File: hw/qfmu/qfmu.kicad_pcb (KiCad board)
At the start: 2 copper layers, 1 part, among them U1 EFM32GG11B120F2048GQ64

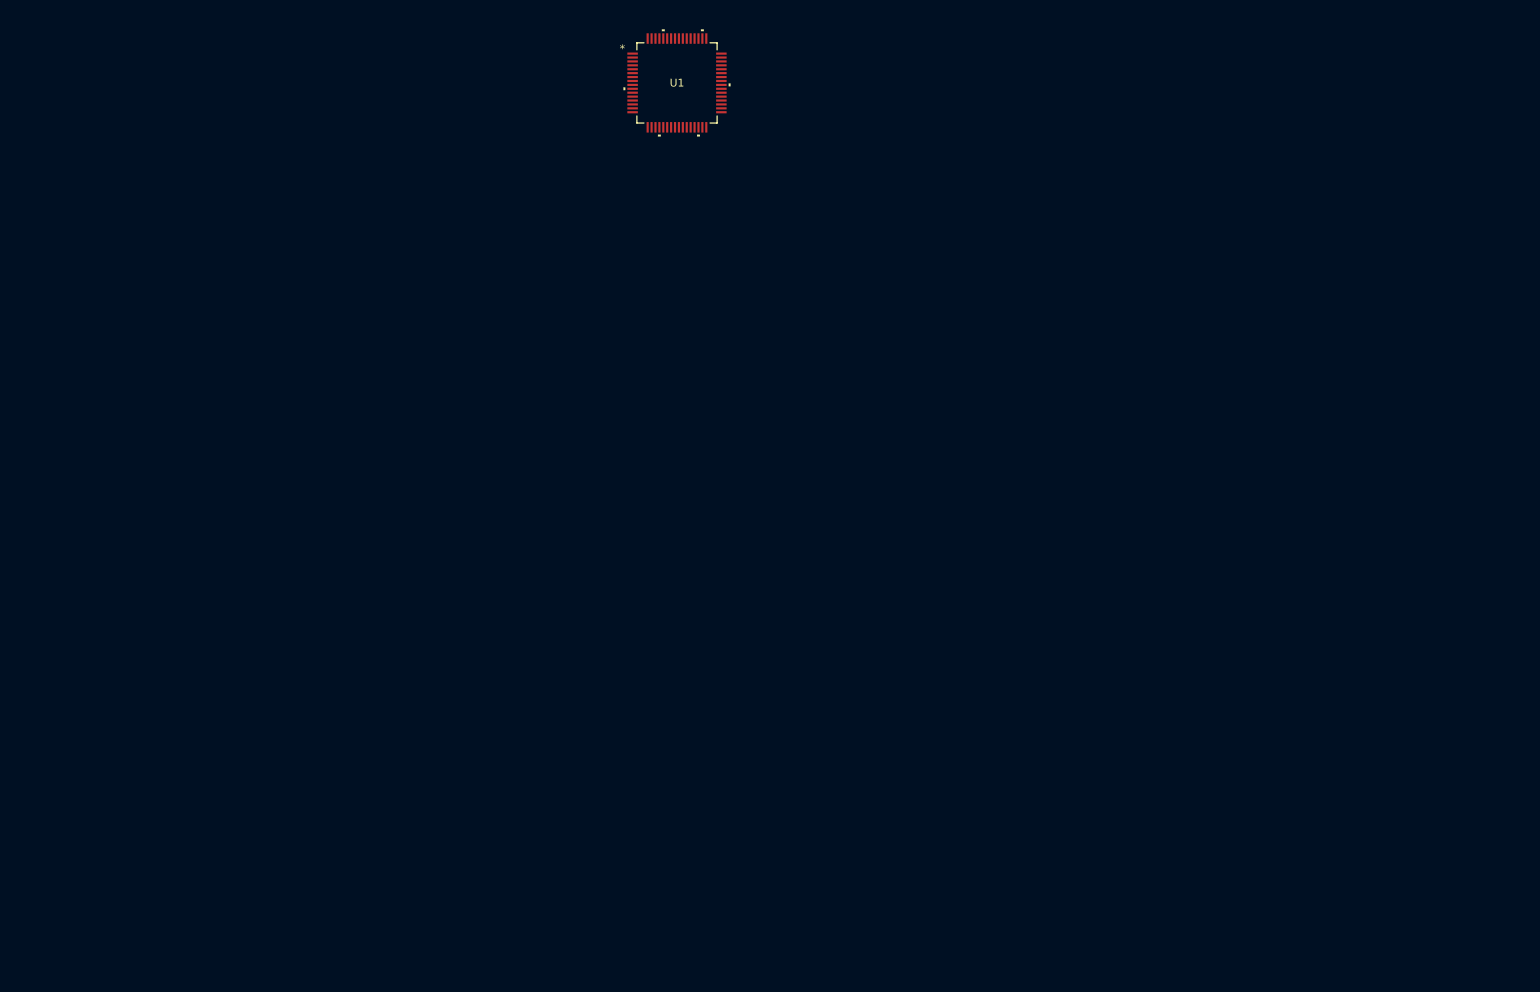
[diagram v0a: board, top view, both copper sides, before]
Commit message: feat: add new BLDC controler and RF section
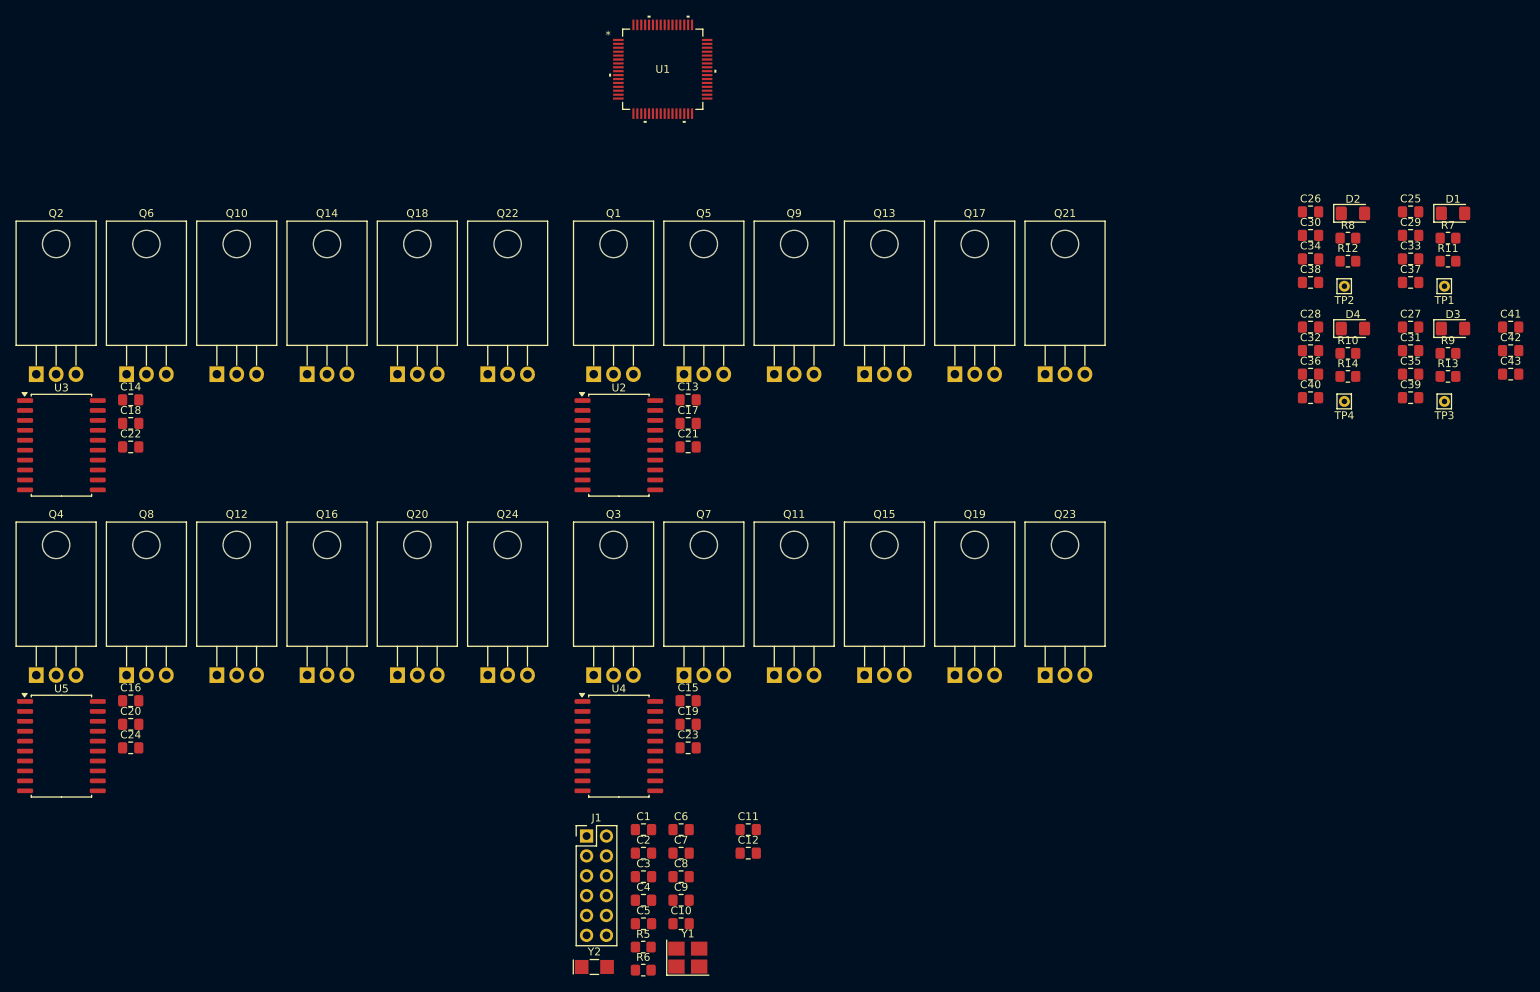
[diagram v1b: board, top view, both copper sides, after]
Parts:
- added C1: 1u, Capacitor_SMD:C_0805_2012Metric_Pad1.18x1.45mm_HandSolder, F.Cu at (132.5, 159.8)
- added C10: 1u, Capacitor_SMD:C_0805_2012Metric_Pad1.18x1.45mm_HandSolder, F.Cu at (137.3, 171.8)
- added C11: 0.1u, Capacitor_SMD:C_0805_2012Metric_Pad1.18x1.45mm_HandSolder, F.Cu at (145.9, 159.8)
- added C12: 0.1u, Capacitor_SMD:C_0805_2012Metric_Pad1.18x1.45mm_HandSolder, F.Cu at (145.9, 162.8)
- added C13: 1u, Capacitor_SMD:C_0805_2012Metric_Pad1.18x1.45mm_HandSolder, F.Cu at (138.2, 104.8)
- added C14: 1u, Capacitor_SMD:C_0805_2012Metric_Pad1.18x1.45mm_HandSolder, F.Cu at (67.0, 104.8)
- added C15: 1u, Capacitor_SMD:C_0805_2012Metric_Pad1.18x1.45mm_HandSolder, F.Cu at (138.2, 143.3)
- added C16: 1u, Capacitor_SMD:C_0805_2012Metric_Pad1.18x1.45mm_HandSolder, F.Cu at (67.0, 143.3)
- added C17: 1u, Capacitor_SMD:C_0805_2012Metric_Pad1.18x1.45mm_HandSolder, F.Cu at (138.2, 107.8)
- added C18: 1u, Capacitor_SMD:C_0805_2012Metric_Pad1.18x1.45mm_HandSolder, F.Cu at (67.0, 107.8)
- added C19: 1u, Capacitor_SMD:C_0805_2012Metric_Pad1.18x1.45mm_HandSolder, F.Cu at (138.2, 146.3)
- added C2: 0.1u, Capacitor_SMD:C_0805_2012Metric_Pad1.18x1.45mm_HandSolder, F.Cu at (132.5, 162.8)
- added C20: 1u, Capacitor_SMD:C_0805_2012Metric_Pad1.18x1.45mm_HandSolder, F.Cu at (67.0, 146.3)
- added C21: 10n, Capacitor_SMD:C_0805_2012Metric_Pad1.18x1.45mm_HandSolder, F.Cu at (138.2, 110.8)
- added C22: 10n, Capacitor_SMD:C_0805_2012Metric_Pad1.18x1.45mm_HandSolder, F.Cu at (67.0, 110.8)
- added C23: 10n, Capacitor_SMD:C_0805_2012Metric_Pad1.18x1.45mm_HandSolder, F.Cu at (138.2, 149.3)
- added C24: 10n, Capacitor_SMD:C_0805_2012Metric_Pad1.18x1.45mm_HandSolder, F.Cu at (67.0, 149.3)
- added C25: 2.2n, Capacitor_SMD:C_0805_2012Metric_Pad1.18x1.45mm_HandSolder, F.Cu at (230.7, 80.7)
- added C26: 2.2n, Capacitor_SMD:C_0805_2012Metric_Pad1.18x1.45mm_HandSolder, F.Cu at (217.9, 80.7)
- added C27: 2.2n, Capacitor_SMD:C_0805_2012Metric_Pad1.18x1.45mm_HandSolder, F.Cu at (230.7, 95.5)
- added C28: 2.2n, Capacitor_SMD:C_0805_2012Metric_Pad1.18x1.45mm_HandSolder, F.Cu at (217.9, 95.5)
- added C29: 4.7n, Capacitor_SMD:C_0805_2012Metric_Pad1.18x1.45mm_HandSolder, F.Cu at (230.7, 83.8)
- added C3: 10u, Capacitor_SMD:C_0805_2012Metric_Pad1.18x1.45mm_HandSolder, F.Cu at (132.5, 165.8)
- added C30: 4.7n, Capacitor_SMD:C_0805_2012Metric_Pad1.18x1.45mm_HandSolder, F.Cu at (217.9, 83.8)
- added C31: 4.7n, Capacitor_SMD:C_0805_2012Metric_Pad1.18x1.45mm_HandSolder, F.Cu at (230.7, 98.5)
- added C32: 4.7n, Capacitor_SMD:C_0805_2012Metric_Pad1.18x1.45mm_HandSolder, F.Cu at (217.9, 98.5)
- added C33: 4.7n, Capacitor_SMD:C_0805_2012Metric_Pad1.18x1.45mm_HandSolder, F.Cu at (230.7, 86.8)
- added C34: 4.7n, Capacitor_SMD:C_0805_2012Metric_Pad1.18x1.45mm_HandSolder, F.Cu at (217.9, 86.8)
- added C35: 4.7n, Capacitor_SMD:C_0805_2012Metric_Pad1.18x1.45mm_HandSolder, F.Cu at (230.7, 101.5)
- added C36: 4.7n, Capacitor_SMD:C_0805_2012Metric_Pad1.18x1.45mm_HandSolder, F.Cu at (217.9, 101.5)
- added C37: 4.7n, Capacitor_SMD:C_0805_2012Metric_Pad1.18x1.45mm_HandSolder, F.Cu at (230.7, 89.8)
- added C38: 4.7n, Capacitor_SMD:C_0805_2012Metric_Pad1.18x1.45mm_HandSolder, F.Cu at (217.9, 89.8)
- added C39: 4.7n, Capacitor_SMD:C_0805_2012Metric_Pad1.18x1.45mm_HandSolder, F.Cu at (230.7, 104.5)
- added C4: 10n, Capacitor_SMD:C_0805_2012Metric_Pad1.18x1.45mm_HandSolder, F.Cu at (132.5, 168.8)
- added C40: 4.7n, Capacitor_SMD:C_0805_2012Metric_Pad1.18x1.45mm_HandSolder, F.Cu at (217.9, 104.5)
- added C41: 0.1u, Capacitor_SMD:C_0805_2012Metric_Pad1.18x1.45mm_HandSolder, F.Cu at (243.5, 95.5)
- added C42: 0.1u, Capacitor_SMD:C_0805_2012Metric_Pad1.18x1.45mm_HandSolder, F.Cu at (243.5, 98.5)
- added C43: 1u, Capacitor_SMD:C_0805_2012Metric_Pad1.18x1.45mm_HandSolder, F.Cu at (243.5, 101.5)
- added C5: 10u, Capacitor_SMD:C_0805_2012Metric_Pad1.18x1.45mm_HandSolder, F.Cu at (132.5, 171.8)
- added C6: 10n, Capacitor_SMD:C_0805_2012Metric_Pad1.18x1.45mm_HandSolder, F.Cu at (137.3, 159.8)
- added C7: 0.1u, Capacitor_SMD:C_0805_2012Metric_Pad1.18x1.45mm_HandSolder, F.Cu at (137.3, 162.8)
- added C8: 1u, Capacitor_SMD:C_0805_2012Metric_Pad1.18x1.45mm_HandSolder, F.Cu at (137.3, 165.8)
- added C9: 0.1u, Capacitor_SMD:C_0805_2012Metric_Pad1.18x1.45mm_HandSolder, F.Cu at (137.3, 168.8)
- added D1: LED, LED_SMD:LED_1206_3216Metric_Pad1.42x1.75mm_HandSolder, F.Cu at (236.1, 80.9)
- added D2: LED, LED_SMD:LED_1206_3216Metric_Pad1.42x1.75mm_HandSolder, F.Cu at (223.3, 80.9)
- added D3: LED, LED_SMD:LED_1206_3216Metric_Pad1.42x1.75mm_HandSolder, F.Cu at (236.1, 95.7)
- added D4: LED, LED_SMD:LED_1206_3216Metric_Pad1.42x1.75mm_HandSolder, F.Cu at (223.3, 95.7)
- added J1: Conn_02x06_Counter_Clockwise, Connector_PinHeader_2.54mm:PinHeader_2x06_P2.54mm_Vertical, F.Cu at (125.3, 160.6)
- added Q1: IRF540N, Package_TO_SOT_THT:TO-220-3_Horizontal_TabDown, F.Cu at (126.2, 101.5)
- added Q10: IRF540N, Package_TO_SOT_THT:TO-220-3_Horizontal_TabDown, F.Cu at (78.0, 101.5)
- added Q11: IRF540N, Package_TO_SOT_THT:TO-220-3_Horizontal_TabDown, F.Cu at (149.3, 140.0)
- added Q12: IRF540N, Package_TO_SOT_THT:TO-220-3_Horizontal_TabDown, F.Cu at (78.0, 140.0)
- added Q13: IRF540N, Package_TO_SOT_THT:TO-220-3_Horizontal_TabDown, F.Cu at (160.8, 101.5)
- added Q14: IRF540N, Package_TO_SOT_THT:TO-220-3_Horizontal_TabDown, F.Cu at (89.5, 101.5)
- added Q15: IRF540N, Package_TO_SOT_THT:TO-220-3_Horizontal_TabDown, F.Cu at (160.8, 140.0)
- added Q16: IRF540N, Package_TO_SOT_THT:TO-220-3_Horizontal_TabDown, F.Cu at (89.5, 140.0)
- added Q17: IRF540N, Package_TO_SOT_THT:TO-220-3_Horizontal_TabDown, F.Cu at (172.4, 101.5)
- added Q18: IRF540N, Package_TO_SOT_THT:TO-220-3_Horizontal_TabDown, F.Cu at (101.1, 101.5)
- added Q19: IRF540N, Package_TO_SOT_THT:TO-220-3_Horizontal_TabDown, F.Cu at (172.4, 140.0)
- added Q2: IRF540N, Package_TO_SOT_THT:TO-220-3_Horizontal_TabDown, F.Cu at (54.9, 101.5)
- added Q20: IRF540N, Package_TO_SOT_THT:TO-220-3_Horizontal_TabDown, F.Cu at (101.1, 140.0)
- added Q21: IRF540N, Package_TO_SOT_THT:TO-220-3_Horizontal_TabDown, F.Cu at (183.9, 101.5)
- added Q22: IRF540N, Package_TO_SOT_THT:TO-220-3_Horizontal_TabDown, F.Cu at (112.6, 101.5)
- added Q23: IRF540N, Package_TO_SOT_THT:TO-220-3_Horizontal_TabDown, F.Cu at (183.9, 140.0)
- added Q24: IRF540N, Package_TO_SOT_THT:TO-220-3_Horizontal_TabDown, F.Cu at (112.6, 140.0)
- added Q3: IRF540N, Package_TO_SOT_THT:TO-220-3_Horizontal_TabDown, F.Cu at (126.2, 140.0)
- added Q4: IRF540N, Package_TO_SOT_THT:TO-220-3_Horizontal_TabDown, F.Cu at (54.9, 140.0)
- added Q5: IRF540N, Package_TO_SOT_THT:TO-220-3_Horizontal_TabDown, F.Cu at (137.7, 101.5)
- added Q6: IRF540N, Package_TO_SOT_THT:TO-220-3_Horizontal_TabDown, F.Cu at (66.4, 101.5)
- added Q7: IRF540N, Package_TO_SOT_THT:TO-220-3_Horizontal_TabDown, F.Cu at (137.7, 140.0)
- added Q8: IRF540N, Package_TO_SOT_THT:TO-220-3_Horizontal_TabDown, F.Cu at (66.4, 140.0)
- added Q9: IRF540N, Package_TO_SOT_THT:TO-220-3_Horizontal_TabDown, F.Cu at (149.3, 101.5)
- added R10: 4.7k, Resistor_SMD:R_0805_2012Metric_Pad1.20x1.40mm_HandSolder, F.Cu at (222.6, 98.8)
- added R11: 4.7k, Resistor_SMD:R_0805_2012Metric_Pad1.20x1.40mm_HandSolder, F.Cu at (235.4, 87.0)
- added R12: 4.7k, Resistor_SMD:R_0805_2012Metric_Pad1.20x1.40mm_HandSolder, F.Cu at (222.6, 87.0)
- added R13: 4.7k, Resistor_SMD:R_0805_2012Metric_Pad1.20x1.40mm_HandSolder, F.Cu at (235.4, 101.8)
- added R14: 4.7k, Resistor_SMD:R_0805_2012Metric_Pad1.20x1.40mm_HandSolder, F.Cu at (222.6, 101.8)
- added R5: 4.7k, Resistor_SMD:R_0805_2012Metric_Pad1.20x1.40mm_HandSolder, F.Cu at (132.5, 174.8)
- added R6: 4.7k, Resistor_SMD:R_0805_2012Metric_Pad1.20x1.40mm_HandSolder, F.Cu at (132.5, 177.7)
- added R7: 4.7k, Resistor_SMD:R_0805_2012Metric_Pad1.20x1.40mm_HandSolder, F.Cu at (235.4, 84.1)
- added R8: 4.7k, Resistor_SMD:R_0805_2012Metric_Pad1.20x1.40mm_HandSolder, F.Cu at (222.6, 84.1)
- added R9: 4.7k, Resistor_SMD:R_0805_2012Metric_Pad1.20x1.40mm_HandSolder, F.Cu at (235.4, 98.8)
- added TP1: TestPoint, Connector_Pin:Pin_D0.7mm_L6.5mm_W1.8mm_FlatFork, F.Cu at (235.0, 90.2)
- added TP2: TestPoint, Connector_Pin:Pin_D0.7mm_L6.5mm_W1.8mm_FlatFork, F.Cu at (222.2, 90.2)
- added TP3: TestPoint, Connector_Pin:Pin_D0.7mm_L6.5mm_W1.8mm_FlatFork, F.Cu at (235.0, 105.0)
- added TP4: TestPoint, Connector_Pin:Pin_D0.7mm_L6.5mm_W1.8mm_FlatFork, F.Cu at (222.2, 105.0)
- added U2: FAN7888, Package_SO:SOIC-20W_7.5x12.8mm_P1.27mm, F.Cu at (129.4, 110.6)
- added U3: FAN7888, Package_SO:SOIC-20W_7.5x12.8mm_P1.27mm, F.Cu at (58.1, 110.6)
- added U4: FAN7888, Package_SO:SOIC-20W_7.5x12.8mm_P1.27mm, F.Cu at (129.4, 149.1)
- added U5: FAN7888, Package_SO:SOIC-20W_7.5x12.8mm_P1.27mm, F.Cu at (58.1, 149.1)
- added Y1: Crystal_GND24, Crystal:Crystal_SMD_3225-4Pin_3.2x2.5mm_HandSoldering, F.Cu at (138.2, 176.1)
- added Y2: Crystal, Crystal:Crystal_SMD_EuroQuartz_EQ161-2Pin_3.2x1.5mm_HandSoldering, F.Cu at (126.3, 177.3)
- moved U1 2.53 mm to (135.0, 62.5)
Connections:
- U1 pad 15: unconnected-(U1-PB7-Pad15) -> /Microcontroller/LFXTAL_P
- U1 pad 16: unconnected-(U1-PB8-Pad16) -> /Microcontroller/LFXTAL_N
- U1 pad 20: unconnected-(U1-RESETn-Pad20) -> /Microcontroller/RESETN
- U1 pad 22: unconnected-(U1-VSS-Pad22) -> GND
- U1 pad 23: unconnected-(U1-AVDD-Pad23) -> +3.3V
- U1 pad 24: unconnected-(U1-PB13-Pad24) -> /Microcontroller/HFXTAL_P
- U1 pad 25: unconnected-(U1-PB14-Pad25) -> /Microcontroller/HFXTAL_N
- U1 pad 26: unconnected-(U1-IOVDD0-Pad26) -> +3.3V
- U1 pad 27: unconnected-(U1-AVDD-Pad27) -> +3.3V
- U1 pad 39: unconnected-(U1-DVDD-Pad39) -> Net-(U1-DVDD)
- U1 pad 40: unconnected-(U1-DECOUPLE-Pad40) -> +3.3V
- U1 pad 41: unconnected-(U1-PC8-Pad41) -> /Microcontroller/SPI_CS
- U1 pad 42: unconnected-(U1-PC9-Pad42) -> /Microcontroller/SPI_CLK
- U1 pad 43: unconnected-(U1-PC10-Pad43) -> /Microcontroller/SPI_MISO
- U1 pad 44: unconnected-(U1-PC11-Pad44) -> /Microcontroller/SPI_MOSI
- U1 pad 45: unconnected-(U1-PC12-Pad45) -> /Microcontroller/I2C2_SDA
- U1 pad 46: unconnected-(U1-PC13-Pad46) -> /Microcontroller/I2C2_SCL
- U1 pad 49: unconnected-(U1-PF0-Pad49) -> /Microcontroller/SWDCLK/TCLK
- U1 pad 50: unconnected-(U1-PF1-Pad50) -> /Microcontroller/SWDIO/TMS
- U1 pad 51: unconnected-(U1-PF2-Pad51) -> /Microcontroller/SWO/TDO
- U1 pad 54: unconnected-(U1-PF5-Pad54) -> /Microcontroller/TDI
- U1 pad 55: unconnected-(U1-IOVDD0-Pad55) -> +3.3V
- U1 pad 56: unconnected-(U1-VSS-Pad56) -> GND
- U1 pad 7: unconnected-(U1-IOVDD0-Pad7) -> +3.3V
- U1 pad 8: unconnected-(U1-VSS-Pad8) -> GND

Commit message: feat: finish motors, RF and power monitor
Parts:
- removed U2, U3, U4, U5: FAN7888, Package_SO:SOIC-20W_7.5x12.8mm_P1.27mm
- added C44: 10p, Capacitor_SMD:C_0805_2012Metric_Pad1.18x1.45mm_HandSolder, F.Cu at (28.9, 128.3)
- added C45: 10p, Capacitor_SMD:C_0805_2012Metric_Pad1.18x1.45mm_HandSolder, F.Cu at (28.9, 131.3)
- added C46: 10p, Capacitor_SMD:C_0805_2012Metric_Pad1.18x1.45mm_HandSolder, F.Cu at (28.9, 134.3)
- added C47: 10p, Capacitor_SMD:C_0805_2012Metric_Pad1.18x1.45mm_HandSolder, F.Cu at (28.9, 137.3)
- added C48: 100p, Capacitor_SMD:C_0805_2012Metric_Pad1.18x1.45mm_HandSolder, F.Cu at (28.9, 140.3)
- added C49: 10u, Capacitor_SMD:C_0805_2012Metric_Pad1.18x1.45mm_HandSolder, F.Cu at (33.7, 128.3)
- added C50: 0.1u, Capacitor_SMD:C_0805_2012Metric_Pad1.18x1.45mm_HandSolder, F.Cu at (33.7, 131.3)
- added C51: 12p, Capacitor_SMD:C_0603_1608Metric_Pad1.08x0.95mm_HandSolder, F.Cu at (43.0, 128.0)
- added C52: 4.7p, Capacitor_SMD:C_0603_1608Metric_Pad1.08x0.95mm_HandSolder, F.Cu at (43.0, 130.5)
- added C53: 2.2u, Capacitor_SMD:C_0805_2012Metric_Pad1.18x1.45mm_HandSolder, F.Cu at (33.7, 134.3)
- added C54: 1.2p, Capacitor_SMD:C_0603_1608Metric_Pad1.08x0.95mm_HandSolder, F.Cu at (43.0, 133.0)
- added C55: 1.5p, Capacitor_SMD:C_0603_1608Metric_Pad1.08x0.95mm_HandSolder, F.Cu at (43.0, 135.5)
- added C56: 0.22u, Capacitor_SMD:C_0805_2012Metric_Pad1.18x1.45mm_HandSolder, F.Cu at (114.3, 131.9)
- added C57: 0.22u, Capacitor_SMD:C_0805_2012Metric_Pad1.18x1.45mm_HandSolder, F.Cu at (114.3, 134.9)
- added C58: 0.22u, Capacitor_SMD:C_0805_2012Metric_Pad1.18x1.45mm_HandSolder, F.Cu at (114.3, 137.9)
- added C59: 0.22u, Capacitor_SMD:C_0805_2012Metric_Pad1.18x1.45mm_HandSolder, F.Cu at (114.3, 141.0)
- added C60: 1u, Capacitor_SMD:C_0805_2012Metric_Pad1.18x1.45mm_HandSolder, F.Cu at (114.3, 144.0)
- added C61: 100p, Capacitor_SMD:C_0805_2012Metric_Pad1.18x1.45mm_HandSolder, F.Cu at (114.3, 147.0)
- added C62: 0.47u, Capacitor_SMD:C_0805_2012Metric_Pad1.18x1.45mm_HandSolder, F.Cu at (119.2, 131.9)
- added C63: 0.1u, Capacitor_SMD:C_0805_2012Metric_Pad1.18x1.45mm_HandSolder, F.Cu at (119.2, 134.9)
- added C64: 100p, Capacitor_SMD:C_0805_2012Metric_Pad1.18x1.45mm_HandSolder, F.Cu at (119.2, 137.9)
- added C65: 0.22u, Capacitor_SMD:C_0805_2012Metric_Pad1.18x1.45mm_HandSolder, F.Cu at (119.2, 141.0)
- added C66: 1u, Capacitor_SMD:C_0805_2012Metric_Pad1.18x1.45mm_HandSolder, F.Cu at (119.2, 144.0)
- added C67: 10u, Capacitor_SMD:C_0805_2012Metric_Pad1.18x1.45mm_HandSolder, F.Cu at (119.2, 147.0)
- added C68: 10u, Capacitor_SMD:C_0805_2012Metric_Pad1.18x1.45mm_HandSolder, F.Cu at (124.0, 131.9)
- added C69: 0.1u, Capacitor_SMD:C_0805_2012Metric_Pad1.18x1.45mm_HandSolder, F.Cu at (124.0, 134.9)
- added C70: 0.1u, Capacitor_SMD:C_0805_2012Metric_Pad1.18x1.45mm_HandSolder, F.Cu at (124.0, 137.9)
- added C71: 22u, Capacitor_SMD:C_0805_2012Metric_Pad1.18x1.45mm_HandSolder, F.Cu at (124.0, 141.0)
- added C72: 22u, Capacitor_SMD:C_0805_2012Metric_Pad1.18x1.45mm_HandSolder, F.Cu at (124.0, 144.0)
- added C73: 220p, Capacitor_SMD:C_0805_2012Metric_Pad1.18x1.45mm_HandSolder, F.Cu at (47.6, 96.3)
- added C74: 220p, Capacitor_SMD:C_0805_2012Metric_Pad1.18x1.45mm_HandSolder, F.Cu at (47.6, 51.6)
- added C75: 220p, Capacitor_SMD:C_0805_2012Metric_Pad1.18x1.45mm_HandSolder, F.Cu at (118.9, 96.3)
- added C76: 220p, Capacitor_SMD:C_0805_2012Metric_Pad1.18x1.45mm_HandSolder, F.Cu at (118.9, 51.6)
- added C77: 1u, Capacitor_SMD:C_0805_2012Metric_Pad1.18x1.45mm_HandSolder, F.Cu at (52.4, 87.3)
- added C78: 1u, Capacitor_SMD:C_0805_2012Metric_Pad1.18x1.45mm_HandSolder, F.Cu at (52.4, 42.6)
- added C79: 1u, Capacitor_SMD:C_0805_2012Metric_Pad1.18x1.45mm_HandSolder, F.Cu at (123.7, 87.3)
- added C80: 1u, Capacitor_SMD:C_0805_2012Metric_Pad1.18x1.45mm_HandSolder, F.Cu at (123.7, 42.6)
- added C81: 0.1u, Capacitor_SMD:C_0805_2012Metric_Pad1.18x1.45mm_HandSolder, F.Cu at (52.4, 90.3)
- added C82: 0.1u, Capacitor_SMD:C_0805_2012Metric_Pad1.18x1.45mm_HandSolder, F.Cu at (52.4, 45.6)
- added C83: 0.1u, Capacitor_SMD:C_0805_2012Metric_Pad1.18x1.45mm_HandSolder, F.Cu at (123.7, 90.3)
- added C84: 0.1u, Capacitor_SMD:C_0805_2012Metric_Pad1.18x1.45mm_HandSolder, F.Cu at (123.7, 45.6)
- added C85: 0.1u, Capacitor_SMD:C_0805_2012Metric_Pad1.18x1.45mm_HandSolder, F.Cu at (52.4, 93.3)
- added C86: 0.1u, Capacitor_SMD:C_0805_2012Metric_Pad1.18x1.45mm_HandSolder, F.Cu at (52.4, 48.6)
- added C87: 0.1u, Capacitor_SMD:C_0805_2012Metric_Pad1.18x1.45mm_HandSolder, F.Cu at (123.7, 93.3)
- added C88: 0.1u, Capacitor_SMD:C_0805_2012Metric_Pad1.18x1.45mm_HandSolder, F.Cu at (123.7, 48.6)
- added C89: 0.1u, Capacitor_SMD:C_0805_2012Metric_Pad1.18x1.45mm_HandSolder, F.Cu at (52.4, 96.3)
- added C90: 0.1u, Capacitor_SMD:C_0805_2012Metric_Pad1.18x1.45mm_HandSolder, F.Cu at (52.4, 51.6)
- added C91: 0.1u, Capacitor_SMD:C_0805_2012Metric_Pad1.18x1.45mm_HandSolder, F.Cu at (123.7, 96.3)
- added C92: 0.1u, Capacitor_SMD:C_0805_2012Metric_Pad1.18x1.45mm_HandSolder, F.Cu at (123.7, 51.6)
- added D5: D_Schottky, Diode_SMD:D_SOD-123, F.Cu at (133.6, 137.0)
- added D6: D_Schottky, Diode_SMD:D_SOD-123, F.Cu at (133.6, 140.3)
- added J2: Conn_Coaxial, Connector_Coaxial:SMA_Amphenol_901-144_Vertical, F.Cu at (49.9, 131.5)
- added J3: Conn_01x03_Pin, Connector_Phoenix_SPT:PhoenixContact_SPT_1.5_3-H-3.5_1x03_P3.5mm_Horizontal, F.Cu at (28.7, 89.8)
- added J4: Conn_01x03_Pin, Connector_Phoenix_SPT:PhoenixContact_SPT_1.5_3-H-3.5_1x03_P3.5mm_Horizontal, F.Cu at (28.7, 45.1)
- added J5: Conn_01x03_Pin, Connector_Phoenix_SPT:PhoenixContact_SPT_1.5_3-H-3.5_1x03_P3.5mm_Horizontal, F.Cu at (100.0, 89.8)
- added J6: Conn_01x03_Pin, Connector_Phoenix_SPT:PhoenixContact_SPT_1.5_3-H-3.5_1x03_P3.5mm_Horizontal, F.Cu at (100.0, 45.1)
- added L1: 470n, Inductor_SMD:L_0402_1005Metric_Pad0.77x0.64mm_HandSolder, F.Cu at (51.6, 122.6)
- added L2: 68n, Inductor_SMD:L_0603_1608Metric_Pad1.05x0.95mm_HandSolder, F.Cu at (43.0, 138.1)
- added L3: 39n, Inductor_SMD:L_0402_1005Metric_Pad0.77x0.64mm_HandSolder, F.Cu at (51.6, 124.6)
- added L4: 33n, Inductor_SMD:L_0603_1608Metric_Pad1.05x0.95mm_HandSolder, F.Cu at (43.0, 140.6)
- added Q25: AO3401A, Package_TO_SOT_SMD:SOT-23, F.Cu at (52.4, 110.8)
- added Q26: AO3400A, Package_TO_SOT_SMD:SOT-23, F.Cu at (52.4, 115.4)
- added Q27: IRF540N, Package_TO_SOT_THT:TO-220-3_Horizontal_TabDown, F.Cu at (96.2, 128.6)
- added Q29: IRF540N, Package_TO_SOT_THT:TO-220-3_Horizontal_TabDown, F.Cu at (107.7, 128.6)
- added Q30: IRF540N, Package_TO_SOT_THT:TO-220-3_Horizontal_TabDown, F.Cu at (119.3, 128.6)
- added Q31: IRF540N, Package_TO_SOT_THT:TO-220-3_Horizontal_TabDown, F.Cu at (130.8, 128.6)
- added R1: 0, Resistor_SMD:R_0805_2012Metric_Pad1.20x1.40mm_HandSolder, F.Cu at (38.5, 128.2)
- added R17: 100k, Resistor_SMD:R_0805_2012Metric_Pad1.20x1.40mm_HandSolder, F.Cu at (38.5, 134.1)
- added R18: 100k, Resistor_SMD:R_0805_2012Metric_Pad1.20x1.40mm_HandSolder, F.Cu at (38.5, 137.1)
- added R19: 10, Resistor_SMD:R_0805_2012Metric_Pad1.20x1.40mm_HandSolder, F.Cu at (38.5, 140.0)
- added R2: 1, Resistor_SMD:R_0805_2012Metric_Pad1.20x1.40mm_HandSolder, F.Cu at (24.0, 87.2)
- added R20: 5m, Resistor_SMD:R_2512_6332Metric_Pad1.40x3.35mm_HandSolder, F.Cu at (130.9, 132.9)
- added R21: 20, Resistor_SMD:R_0805_2012Metric_Pad1.20x1.40mm_HandSolder, F.Cu at (95.3, 131.9)
- added R22: 20, Resistor_SMD:R_0805_2012Metric_Pad1.20x1.40mm_HandSolder, F.Cu at (95.3, 134.8)
- added R23: 20, Resistor_SMD:R_0805_2012Metric_Pad1.20x1.40mm_HandSolder, F.Cu at (95.3, 137.8)
- added R24: 20, Resistor_SMD:R_0805_2012Metric_Pad1.20x1.40mm_HandSolder, F.Cu at (95.3, 140.7)
- added R25: 100, Resistor_SMD:R_0805_2012Metric_Pad1.20x1.40mm_HandSolder, F.Cu at (95.3, 143.7)
- added R26: 100, Resistor_SMD:R_0805_2012Metric_Pad1.20x1.40mm_HandSolder, F.Cu at (100.1, 131.9)
- added R27: 100, Resistor_SMD:R_0805_2012Metric_Pad1.20x1.40mm_HandSolder, F.Cu at (100.1, 134.8)
- added R28: 10k, Resistor_SMD:R_0805_2012Metric_Pad1.20x1.40mm_HandSolder, F.Cu at (100.1, 137.8)
- added R29: 10k, Resistor_SMD:R_0805_2012Metric_Pad1.20x1.40mm_HandSolder, F.Cu at (100.1, 140.7)
- added R3: 0, Resistor_SMD:R_0805_2012Metric_Pad1.20x1.40mm_HandSolder, F.Cu at (38.5, 131.2)
- added R30: 10M, Resistor_SMD:R_0805_2012Metric_Pad1.20x1.40mm_HandSolder, F.Cu at (100.1, 143.7)
- added R31: 10M, Resistor_SMD:R_0805_2012Metric_Pad1.20x1.40mm_HandSolder, F.Cu at (104.8, 131.9)
- added R32: 10M, Resistor_SMD:R_0805_2012Metric_Pad1.20x1.40mm_HandSolder, F.Cu at (104.8, 134.8)
- added R33: 10M, Resistor_SMD:R_0805_2012Metric_Pad1.20x1.40mm_HandSolder, F.Cu at (104.8, 137.8)
- added R34: 3.9k, Resistor_SMD:R_0805_2012Metric_Pad1.20x1.40mm_HandSolder, F.Cu at (104.8, 140.7)
- added R35: 3.9k, Resistor_SMD:R_0805_2012Metric_Pad1.20x1.40mm_HandSolder, F.Cu at (104.8, 143.7)
- added R36: 10k, Resistor_SMD:R_0805_2012Metric_Pad1.20x1.40mm_HandSolder, F.Cu at (109.6, 131.9)
- added R37: 10k, Resistor_SMD:R_0805_2012Metric_Pad1.20x1.40mm_HandSolder, F.Cu at (109.6, 134.8)
- added R38: 30.9k, Resistor_SMD:R_0805_2012Metric_Pad1.20x1.40mm_HandSolder, F.Cu at (109.6, 137.8)
- added R39: 4.7k, Resistor_SMD:R_0805_2012Metric_Pad1.20x1.40mm_HandSolder, F.Cu at (109.6, 140.7)
- added R4: 1, Resistor_SMD:R_0805_2012Metric_Pad1.20x1.40mm_HandSolder, F.Cu at (24.0, 42.6)
- added R40: 4.7k, Resistor_SMD:R_0805_2012Metric_Pad1.20x1.40mm_HandSolder, F.Cu at (109.6, 143.7)
- added R41: 1, Resistor_SMD:R_0805_2012Metric_Pad1.20x1.40mm_HandSolder, F.Cu at (95.3, 93.1)
- added R42: 1, Resistor_SMD:R_0805_2012Metric_Pad1.20x1.40mm_HandSolder, F.Cu at (95.3, 48.5)
- added R43: 2k, Resistor_SMD:R_0805_2012Metric_Pad1.20x1.40mm_HandSolder, F.Cu at (24.0, 96.1)
- added R44: 2k, Resistor_SMD:R_0805_2012Metric_Pad1.20x1.40mm_HandSolder, F.Cu at (24.0, 51.4)
- added R45: 2k, Resistor_SMD:R_0805_2012Metric_Pad1.20x1.40mm_HandSolder, F.Cu at (95.3, 96.1)
- added R46: 2k, Resistor_SMD:R_0805_2012Metric_Pad1.20x1.40mm_HandSolder, F.Cu at (95.3, 51.4)
- added R47: 10k, Resistor_SMD:R_0805_2012Metric_Pad1.20x1.40mm_HandSolder, F.Cu at (24.0, 99.0)
- added R48: 10k, Resistor_SMD:R_0805_2012Metric_Pad1.20x1.40mm_HandSolder, F.Cu at (24.0, 54.4)
- added R49: 10k, Resistor_SMD:R_0805_2012Metric_Pad1.20x1.40mm_HandSolder, F.Cu at (95.3, 99.0)
- added R50: 10k, Resistor_SMD:R_0805_2012Metric_Pad1.20x1.40mm_HandSolder, F.Cu at (95.3, 54.4)
- added R51: 100k, Resistor_SMD:R_0805_2012Metric_Pad1.20x1.40mm_HandSolder, F.Cu at (24.0, 102.0)
- added R52: 100k, Resistor_SMD:R_0805_2012Metric_Pad1.20x1.40mm_HandSolder, F.Cu at (24.0, 57.3)
- added R53: 100k, Resistor_SMD:R_0805_2012Metric_Pad1.20x1.40mm_HandSolder, F.Cu at (95.3, 102.0)
- added R54: 100k, Resistor_SMD:R_0805_2012Metric_Pad1.20x1.40mm_HandSolder, F.Cu at (95.3, 57.3)
- added R55: 300k, Resistor_SMD:R_0805_2012Metric_Pad1.20x1.40mm_HandSolder, F.Cu at (24.0, 104.9)
- added R56: 300k, Resistor_SMD:R_0805_2012Metric_Pad1.20x1.40mm_HandSolder, F.Cu at (24.0, 60.3)
- added R57: 300k, Resistor_SMD:R_0805_2012Metric_Pad1.20x1.40mm_HandSolder, F.Cu at (95.3, 104.9)
- added R58: 300k, Resistor_SMD:R_0805_2012Metric_Pad1.20x1.40mm_HandSolder, F.Cu at (95.3, 60.3)
- added TH1: Thermistor_NTC, Resistor_SMD:R_0603_1608Metric_Pad0.98x0.95mm_HandSolder, F.Cu at (128.6, 136.6)
- added TH2: Thermistor_NTC, Resistor_SMD:R_0603_1608Metric_Pad0.98x0.95mm_HandSolder, F.Cu at (128.6, 139.1)
- added TH3: Thermistor_NTC, Resistor_SMD:R_0603_1608Metric_Pad0.98x0.95mm_HandSolder, F.Cu at (128.6, 141.6)
- added U12: AS179-92LF, Package_TO_SOT_SMD:SOT-363_SC-70-6, F.Cu at (52.1, 119.7)
- added U14: TPS562202, Package_TO_SOT_SMD:SOT-563, F.Cu at (132.6, 143.8)
- added Y3: 13.52 MHz, Crystal:Crystal_HC49-U_Horizontal, F.Cu at (26.3, 109.9)
- added Y4: 13.52 MHz, Crystal:Crystal_HC49-U_Horizontal, F.Cu at (40.4, 109.9)
- moved C41 222.8 mm to (24.1, 134.3)
- moved C42 222.8 mm to (24.1, 137.3)
- moved C43 222.8 mm to (24.1, 140.3)
- moved R11 211.5 mm to (24.0, 93.1)
- moved R7 211.5 mm to (24.0, 90.2)
- moved R12 202.3 mm to (24.0, 48.5)
- moved R8 202.3 mm to (24.0, 45.5)
- moved D1 193.6 mm to (43.4, 99.5)
- moved TP1 193.1 mm to (42.3, 102.9)
- moved C25 188.6 mm to (42.8, 96.3)
- moved C29 183.1 mm to (47.6, 87.3)
- moved C33 183.1 mm to (47.6, 90.3)
- moved C37 183.1 mm to (47.6, 93.3)
- moved TP2 182.7 mm to (42.3, 58.3)
- moved D2 181.8 mm to (43.4, 54.8)
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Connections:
- C43 pad 2: unconnected-(C43-Pad2) -> GND
- Q1 pad 1: unconnected-(Q1-G-Pad1) -> /Motor 1/HO1
- Q1 pad 2: unconnected-(Q1-D-Pad2) -> +12V
- Q10 pad 1: unconnected-(Q10-G-Pad1) -> /Motor 2/HO3
- Q10 pad 2: unconnected-(Q10-D-Pad2) -> +12V
- Q11 pad 1: unconnected-(Q11-G-Pad1) -> /Motor 3/HO3
- Q11 pad 2: unconnected-(Q11-D-Pad2) -> +12V
- Q12 pad 1: unconnected-(Q12-G-Pad1) -> /Motor 4/HO3
- Q12 pad 2: unconnected-(Q12-D-Pad2) -> +12V
- Q13 pad 1: unconnected-(Q13-G-Pad1) -> /Motor 1/LO1
- Q13 pad 3: GND -> Net-(Q13-S)
- Q14 pad 1: unconnected-(Q14-G-Pad1) -> /Motor 2/LO1
- Q14 pad 3: GND -> Net-(Q14-S)
- Q15 pad 1: unconnected-(Q15-G-Pad1) -> /Motor 3/LO1
- Q15 pad 3: GND -> Net-(Q15-S)
- Q16 pad 1: unconnected-(Q16-G-Pad1) -> /Motor 4/LO1
- Q16 pad 3: GND -> Net-(Q16-S)
- Q17 pad 1: unconnected-(Q17-G-Pad1) -> /Motor 1/LO2
- Q17 pad 3: GND -> Net-(Q13-S)
- Q18 pad 1: unconnected-(Q18-G-Pad1) -> /Motor 2/LO2
- Q18 pad 3: GND -> Net-(Q14-S)
- Q19 pad 1: unconnected-(Q19-G-Pad1) -> /Motor 3/LO2
- Q19 pad 3: GND -> Net-(Q15-S)
- Q2 pad 1: unconnected-(Q2-G-Pad1) -> /Motor 2/HO1
- Q2 pad 2: unconnected-(Q2-D-Pad2) -> +12V
- Q20 pad 1: unconnected-(Q20-G-Pad1) -> /Motor 4/LO2
- Q20 pad 3: GND -> Net-(Q16-S)
- Q21 pad 1: unconnected-(Q21-G-Pad1) -> /Motor 1/LO3
- Q21 pad 3: GND -> Net-(Q13-S)
- Q22 pad 1: unconnected-(Q22-G-Pad1) -> /Motor 2/LO3
- Q22 pad 3: GND -> Net-(Q14-S)
- Q23 pad 1: unconnected-(Q23-G-Pad1) -> /Motor 3/LO3
- Q23 pad 3: GND -> Net-(Q15-S)
- Q24 pad 1: unconnected-(Q24-G-Pad1) -> /Motor 4/LO3
- Q24 pad 3: GND -> Net-(Q16-S)
- Q3 pad 1: unconnected-(Q3-G-Pad1) -> /Motor 3/HO1
- Q3 pad 2: unconnected-(Q3-D-Pad2) -> +12V
- Q4 pad 1: unconnected-(Q4-G-Pad1) -> /Motor 4/HO1
- Q4 pad 2: unconnected-(Q4-D-Pad2) -> +12V
- Q5 pad 1: unconnected-(Q5-G-Pad1) -> /Motor 1/HO2
- Q5 pad 2: unconnected-(Q5-D-Pad2) -> +12V
- Q6 pad 1: unconnected-(Q6-G-Pad1) -> /Motor 2/HO2
- Q6 pad 2: unconnected-(Q6-D-Pad2) -> +12V
- Q7 pad 1: unconnected-(Q7-G-Pad1) -> /Motor 3/HO2
- Q7 pad 2: unconnected-(Q7-D-Pad2) -> +12V
- Q8 pad 1: unconnected-(Q8-G-Pad1) -> /Motor 4/HO2
- Q8 pad 2: unconnected-(Q8-D-Pad2) -> +12V
- Q9 pad 1: unconnected-(Q9-G-Pad1) -> /Motor 1/HO3
- Q9 pad 2: unconnected-(Q9-D-Pad2) -> +12V
